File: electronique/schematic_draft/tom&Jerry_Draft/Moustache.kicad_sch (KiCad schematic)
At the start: 9 parts, among them IC3 IIM-20670, J4 Conn_01x08, J5 Conn_01x04, J6 Conn_01x04, J7 Conn_01x04, J8 Conn_01x04

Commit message: STM32 KiCAD V2 - 18.09.2024
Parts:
- removed C27: 10nF, Capacitor_SMD:C_0603_1608Metric_Pad1.08x0.95mm_HandSolder, symbol Device:C_Small
- removed C28, C29: 100nF, Capacitor_SMD:C_0603_1608Metric_Pad1.08x0.95mm_HandSolder, symbol Device:C_Small
- removed IC3: IIM-20670, Library:IMU, symbol Ludzlib:IIM-20670
- removed J4: Conn_01x08, Connector_JST:JST_XH_S8B-XH-A_1x08_P2.50mm_Horizontal, symbol Connector_Generic:Conn_01x08
- removed J5, J6, J7, J8: Conn_01x04, Connector_JST:JST_XH_S4B-XH-A_1x04_P2.50mm_Horizontal, symbol Connector_Generic:Conn_01x04
- added J301, J303, J304, J305: Conn_01x02, symbol Connector_Generic:Conn_01x02
- added J302: Conn_01x08, symbol Connector_Generic:Conn_01x08
- added U301: ADXL343, Package_LGA:LGA-14_3x5mm_P0.8mm_LayoutBorder1x6y, symbol Sensor_Motion:ADXL343
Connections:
- net +3.3V: now also J301.1 (Pin_1), J303.1 (Pin_1), J304.1 (Pin_1), J305.1 (Pin_1), U301.1 (Vdd_I/O), U301.3 (RES), U301.6 (Vs), U301.7 (~{CS})
- net +5V: now also J302.8 (Pin_8)
- net GND: now also J302.5 (Pin_5), U301.11 (RES), U301.12 (SDO/ADDR), U301.2 (GND), U301.4 (GND), U301.5 (GND)
- net LIDAR_PWM: now also J302.4 (Pin_4)
- net LIDAR_RX: now also J302.6 (Pin_6)
- net LIDAR_TX: now also J302.7 (Pin_7)
- net Moustache_1: now also J301.2 (Pin_2)
- net Moustache_2: now also J303.2 (Pin_2)
- net Moustache_3: now also J304.2 (Pin_2)
- net Moustache_4: now also J305.2 (Pin_2)
- new net IMU_INT1: U301.8 (INT1)
- new net IMU_INT2: U301.9 (INT2)
- new net IMU_SCL: U301.14 (SCL/SCLK)
- new net IMU_SDA: U301.13 (SDA/SDI/SDIO)
- new net LIDAR_DEV_EN: J302.3 (Pin_3)
- new net LIDAR_M_EN: J302.2 (Pin_2)
- no-connect marks 5 -> 1
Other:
- added sheet TOF1 (tof.kicad_sch)
- added sheet TOF2 (tof.kicad_sch)
- added sheet TOF3 (tof.kicad_sch)
- added sheet TOF4 (tof.kicad_sch)
- added sheet TOF5 (tof.kicad_sch)
- added sheet TOF6 (tof.kicad_sch)
- note added: "IMU est seul sur le I2C"
- note added: "TOF"
- note removed: "Edge sensor"
- note removed: "activate pull down/up in STM32"
- note removed: "recommanded capacitor"

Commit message: KiCAD V3 - 18.09.2024
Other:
- note added: "IMU est seul sur le I2C donc CS: ON et ADDR:GND"
- note removed: "IMU est seul sur le I2C"

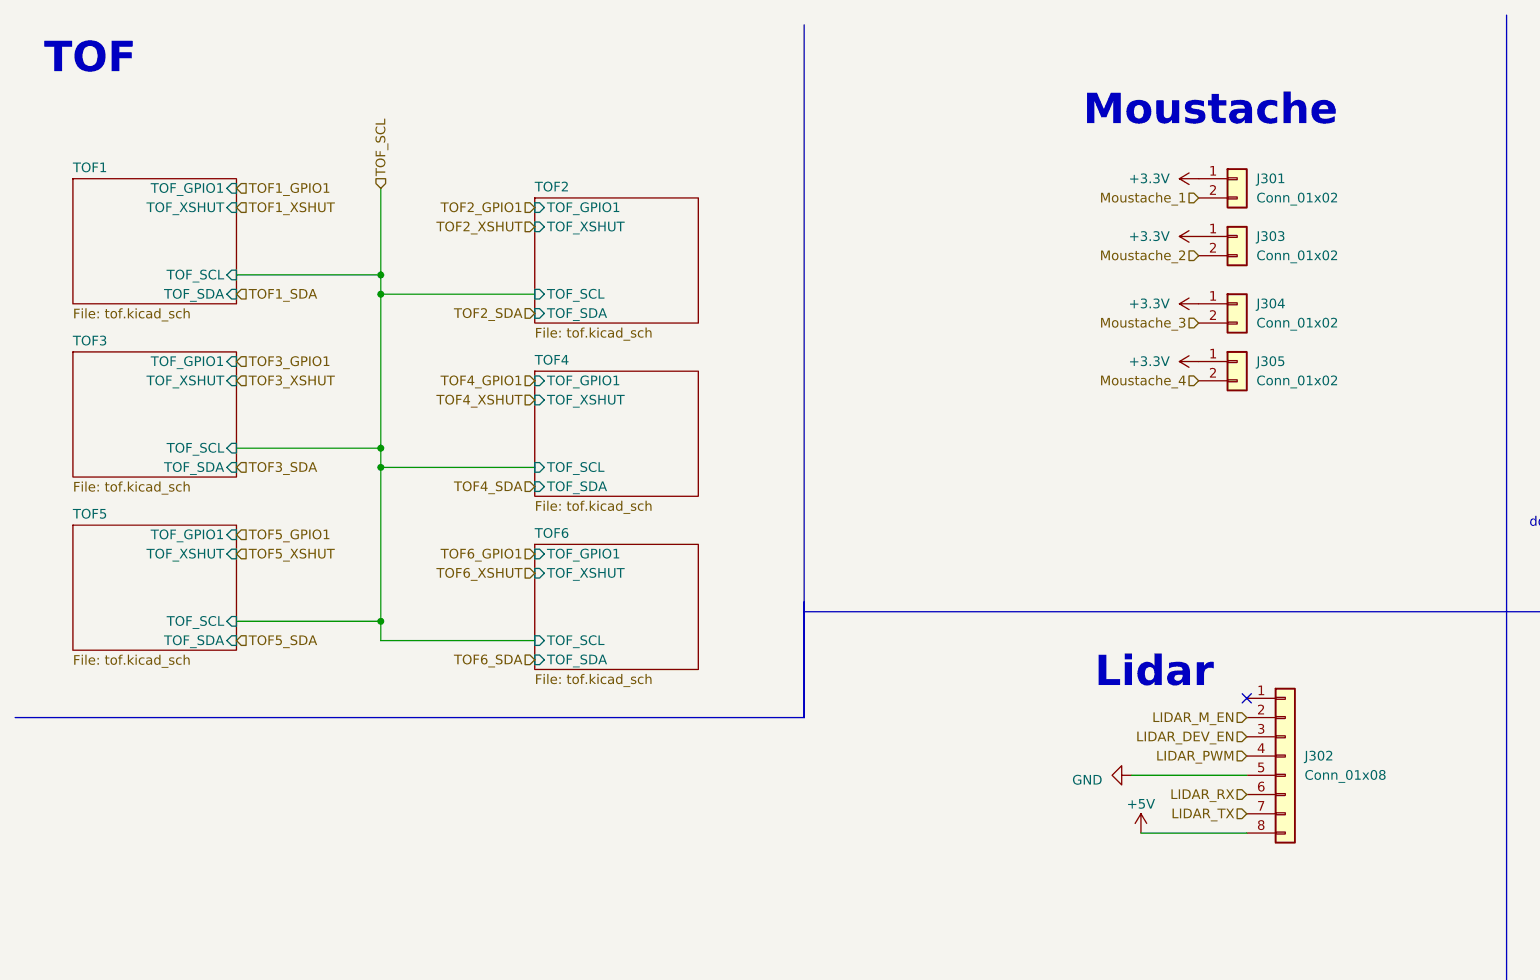
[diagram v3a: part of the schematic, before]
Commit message: STM32 KiCAD V5 - 25.09.2024 - Ajout connecteurs TOF, ...
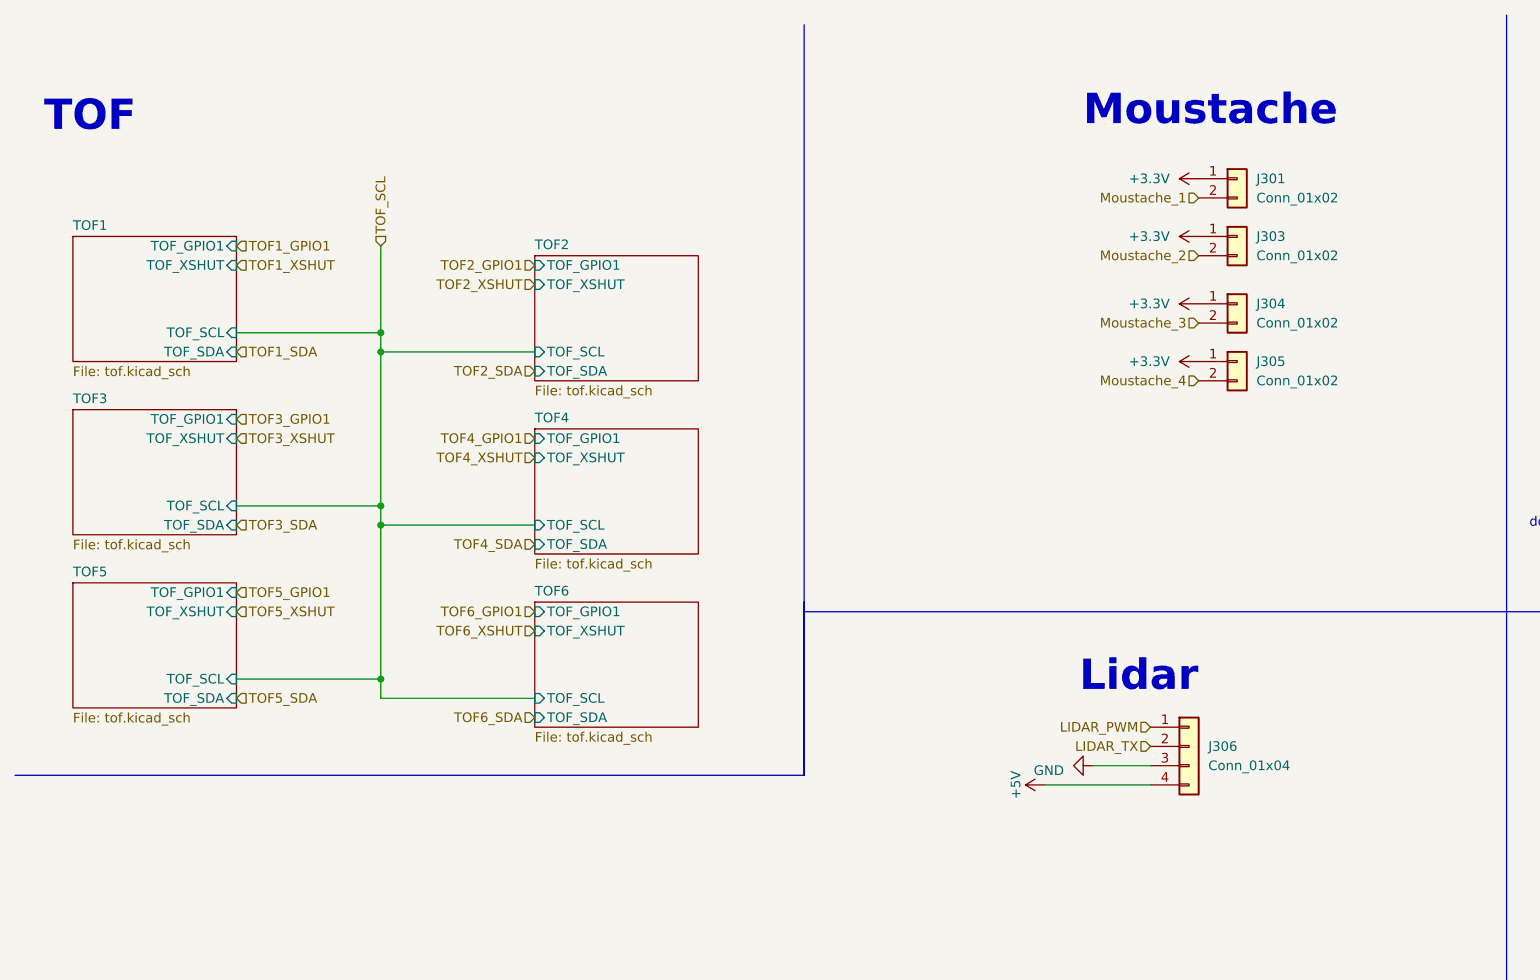
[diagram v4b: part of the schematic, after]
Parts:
- removed J302: Conn_01x08, symbol Connector_Generic:Conn_01x08
- added J306: Conn_01x04, symbol Connector_Generic:Conn_01x04
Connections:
- net +5V: now also J306.4 (Pin_4)
- net GND: now also J306.3 (Pin_3)
- net LIDAR_PWM: now also J306.1 (Pin_1)
- net LIDAR_TX: now also J306.2 (Pin_2)
- no-connect marks 1 -> 0

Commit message: STM32 KiCAD v2.0 x CubeIDE - Pin definitif + schematic reviewed
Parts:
- removed J301, J303, J304, J305: Conn_01x02, symbol Connector_Generic:Conn_01x02
- removed J306: Conn_01x04, symbol Connector_Generic:Conn_01x04
- added C301: 100n, symbol Device:C_Small
- added IC301: TCA9555RTWR, QFN50P400X400X80-25N-D, symbol TCA9555RTWR:TCA9555RTWR
- added J301: Conn_01x08, symbol Connector_Generic:Conn_01x08
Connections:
- net +3.3V: now also C301.1
- net +5V: now also IC301.21 (VCC), J301.8 (Pin_8)
- net GND: now also C301.2, IC301.18 (A0), IC301.23 (A1), IC301.24 (A2), IC301.9 (GND), J301.5 (Pin_5)
- net IMU_INT1: now also IC301.14 (P14)
- net IMU_INT2: now also IC301.15 (P15)
- net LIDAR_TX: now also J301.7 (Pin_7)
- net TOF1_GPIO1: now also IC301.12 (P12)
- net TOF1_XSHUT: now also IC301.13 (P13)
- net TOF2_GPIO1: now also IC301.10 (P10)
- net TOF2_XSHUT: now also IC301.11 (P11)
- net TOF3_GPIO1: now also IC301.7 (P06)
- net TOF3_XSHUT: now also IC301.8 (P07)
- net TOF4_GPIO1: now also IC301.6 (P05)
- net TOF4_XSHUT: now also IC301.5 (P04)
- net TOF5_GPIO1: now also IC301.4 (P03)
- net TOF5_XSHUT: now also IC301.3 (P02)
- net TOF6_GPIO1: now also IC301.2 (P01)
- net TOF6_XSHUT: now also IC301.1 (P00)
- new net EXPANDER_EXTI: IC301.22 (~{INT})
- new net I2C_MAIN_SCL: IC301.19 (SCL)
- new net I2C_MAIN_SDA: IC301.20 (SDA)
- new net LIDAR_DEV_EN: IC301.17 (P17), J301.3 (Pin_3)
- new net LIDAR_M_CTR: J301.4 (Pin_4)
- new net LIDAR_M_EN: IC301.16 (P16), J301.2 (Pin_2)
- new net LIDAR_RX: J301.6 (Pin_6)
- no-connect marks 0 -> 1
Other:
- added sheet Moustache1 (Moustache_out.kicad_sch)
- added sheet Moustache2 (Moustache_out.kicad_sch)
- added sheet Moustache3 (Moustache_out.kicad_sch)
- added sheet Moustache4 (Moustache_out.kicad_sch)
- note added: "Capteurs TOFs"
- note added: "GPIO Expander"
- note added: "Moustaches"
- note removed: "Moustache"
- note removed: "TOF"
- moved on the sheet: U301

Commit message: Adding footprint V0.1
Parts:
- C301: footprint (none) -> Capacitor_SMD:C_0805_2012Metric
- IC301: footprint QFN50P400X400X80-25N-D -> Tom&Jerry:RTW24_2P45X2P45
- J301: footprint (none) -> Connector_JST:JST_XH_S8B-XH-A_1x08_P2.50mm_Horizontal
- U301: footprint Package_LGA:LGA-14_3x5mm_P0.8mm_LayoutBorder1x6y -> Tom&Jerry:PQFN80P300X500X100-14N
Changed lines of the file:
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@@
 			)
 		)
-		(property "Footprint" ""
+		(property "Footprint" "Capacitor_SMD:C_0805_2012Metric"
 			(at 264.16 41.91 0)
 			(effects
@@
 			)
 		)
-		(property "Footprint" "Package_LGA:LGA-14_3x5mm_P0.8mm_LayoutBorder1x6y"
+		(property "Footprint" "Tom&Jerry:PQFN80P300X500X100-14N"
 			(at 243.586 33.782 0)
 			(effects
@@
 			)
 		)
-		(property "Footprint" "QFN50P400X400X80-25N-D"
+		(property "Footprint" "Tom&Jerry:RTW24_2P45X2P45"
 			(at -12.37 167.64 0)
 			(effects
@@
 			)
 		)
-		(property "Footprint" ""
+		(property "Footprint" "Connector_JST:JST_XH_S8B-XH-A_1x08_P2.50mm_Horizontal"
 			(at 248.92 128.27 0)
 			(effects

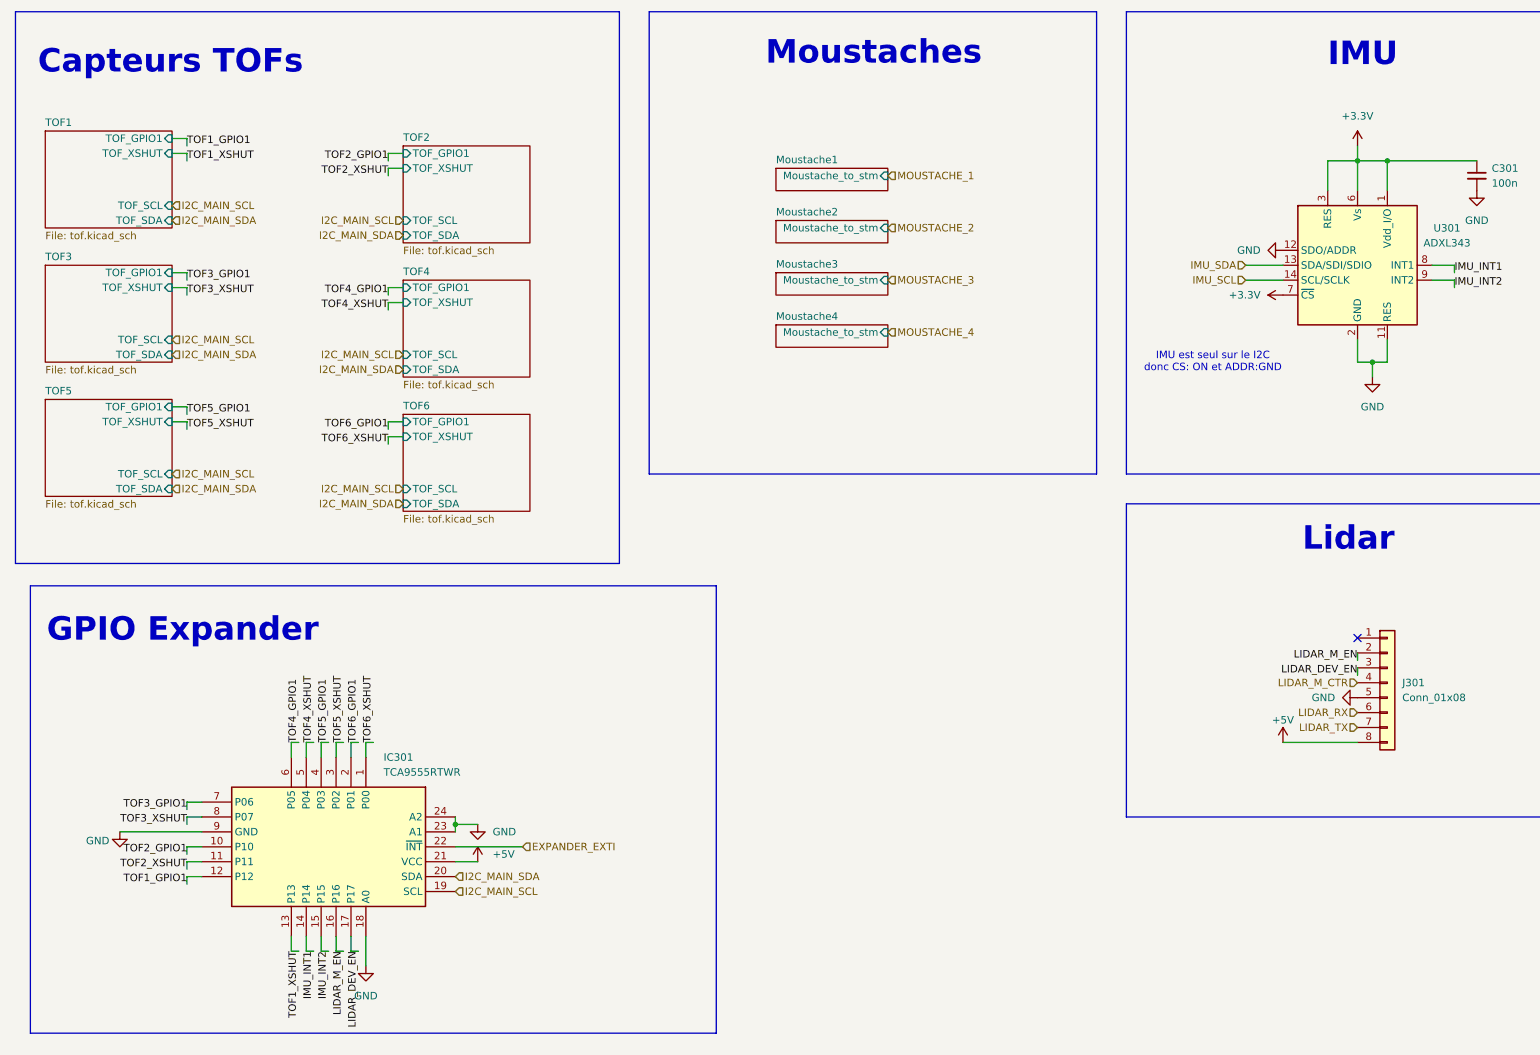
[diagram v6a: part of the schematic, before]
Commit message: Ajout V2 TOF + MultiPCB Panalize
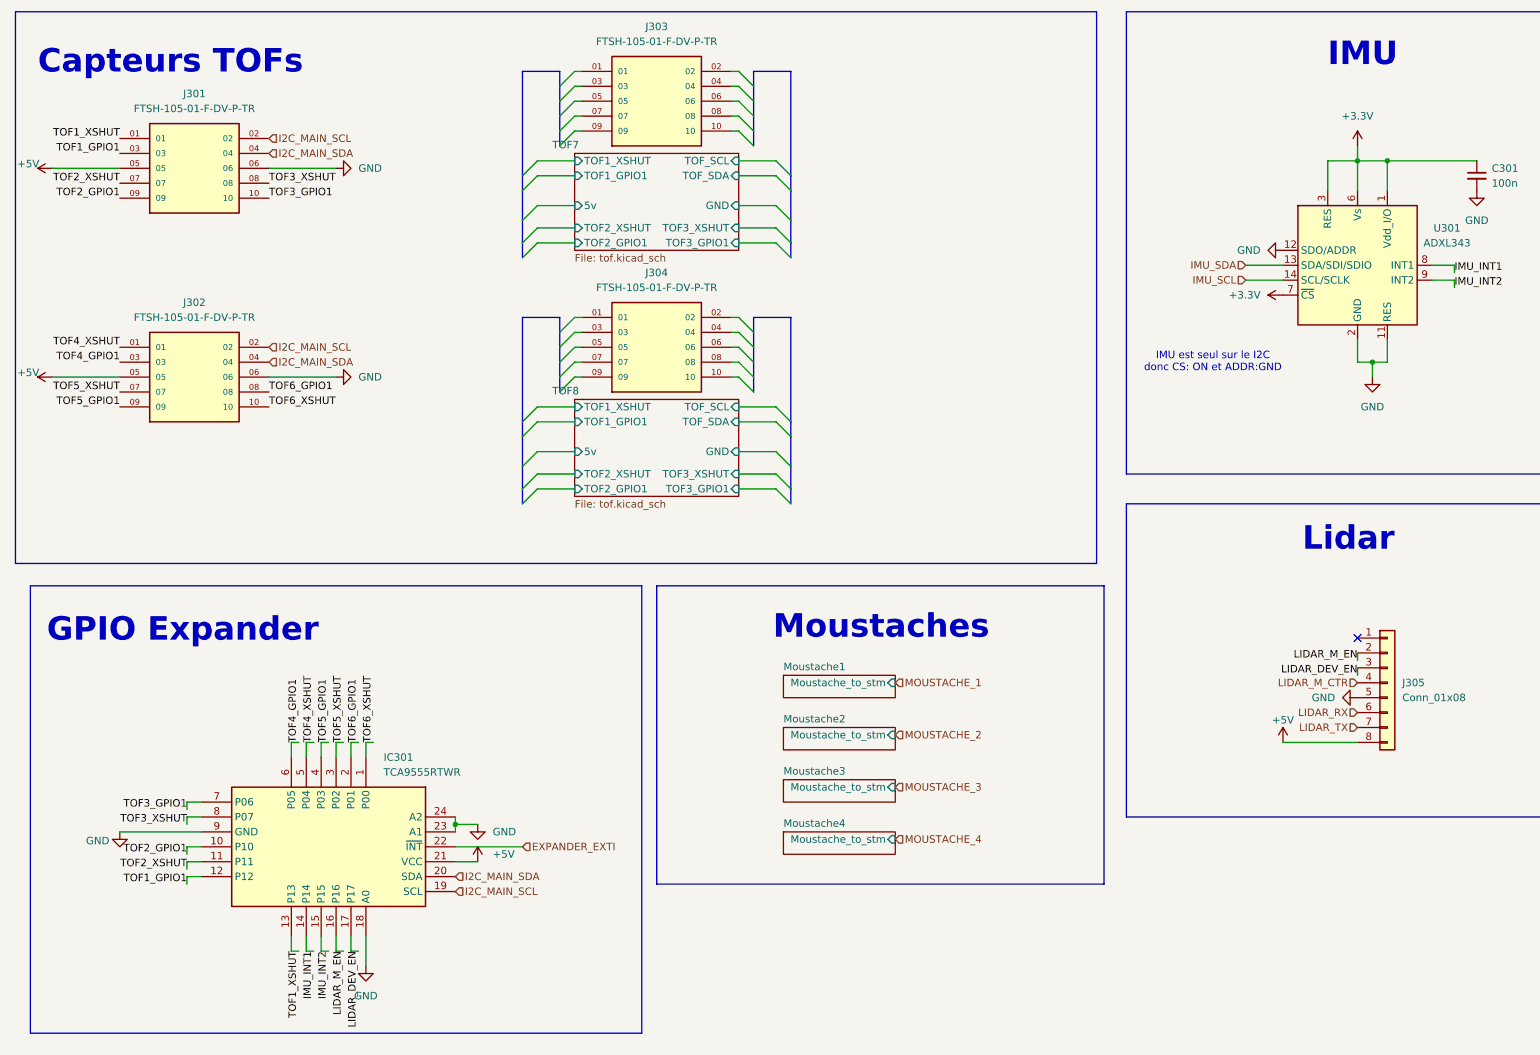
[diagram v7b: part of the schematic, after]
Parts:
- added J301, J302, J303, J304: FTSH-105-01-F-DV-P-TR, Tom&Jerry:SAMTEC_FTSH-105-01-F-DV-P-TR, symbol Tom&Jerry:FTSH-105-01-F-DV-P-TR
- renumbered J301 to J305
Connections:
- net +5V: now also J301.05, J302.05
- net GND: now also J301.06, J302.06
- net I2C_MAIN_SCL: now also J301.02, J302.02
- net I2C_MAIN_SDA: now also J301.04, J302.04
- net TOF1_GPIO1: now also J301.03
- net TOF1_XSHUT: now also J301.01
- net TOF2_GPIO1: now also J301.09
- net TOF2_XSHUT: now also J301.07
- net TOF3_GPIO1: now also J301.10
- net TOF3_XSHUT: now also J301.08
- net TOF4_GPIO1: now also J302.03
- net TOF4_XSHUT: now also J302.01
- net TOF5_GPIO1: now also J302.09
- net TOF5_XSHUT: now also J302.07
- net TOF6_GPIO1: now also J302.08
- net TOF6_XSHUT: now also J302.10
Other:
- removed sheet TOF1
- removed sheet TOF2
- removed sheet TOF3
- removed sheet TOF4
- removed sheet TOF5
- removed sheet TOF6
- added sheet TOF7 (tof.kicad_sch)
- added sheet TOF8 (tof.kicad_sch)

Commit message: Ajout du routage LED + TOF + quelques Via
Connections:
- net I2C_MAIN_SCL: now also J302.08; no longer J302.02
- net I2C_MAIN_SDA: now also J302.10; no longer J302.04
- net IMU_INT1: now also IC301.17 (P17); no longer IC301.14 (P14)
- net IMU_INT2: now also IC301.16 (P16); no longer IC301.15 (P15)
- net LIDAR_DEV_EN: now also IC301.15 (P15); no longer IC301.17 (P17)
- net LIDAR_M_EN: now also IC301.14 (P14); no longer IC301.16 (P16)
- net TOF1_GPIO1: now also IC301.7 (P06); no longer IC301.12 (P12)
- net TOF1_XSHUT: now also IC301.8 (P07); no longer IC301.13 (P13)
- net TOF3_GPIO1: now also IC301.13 (P13); no longer IC301.7 (P06)
- net TOF3_XSHUT: now also IC301.12 (P12); no longer IC301.8 (P07)
- net TOF4_GPIO1: now also IC301.2 (P01); no longer IC301.6 (P05)
- net TOF4_XSHUT: now also IC301.1 (P00); no longer IC301.5 (P04)
- net TOF6_GPIO1: now also IC301.6 (P05), J302.04; no longer IC301.2 (P01), J302.08
- net TOF6_XSHUT: now also IC301.5 (P04), J302.02; no longer IC301.1 (P00), J302.10
